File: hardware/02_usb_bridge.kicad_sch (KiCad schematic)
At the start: 73 parts, among them J201 PCB pads (no component), J202 PCB pads (no component), Q207 AO3400A, U201 CH32V307RCT6, U202 AGRV2KQ32, U205 74LVC1G157, U206 74LVC1G11, U208 74LVC3G34, X201 80.000 MHz, X202 49.152 MHz, X203 45.1584 MHz, Y201 8 MHz

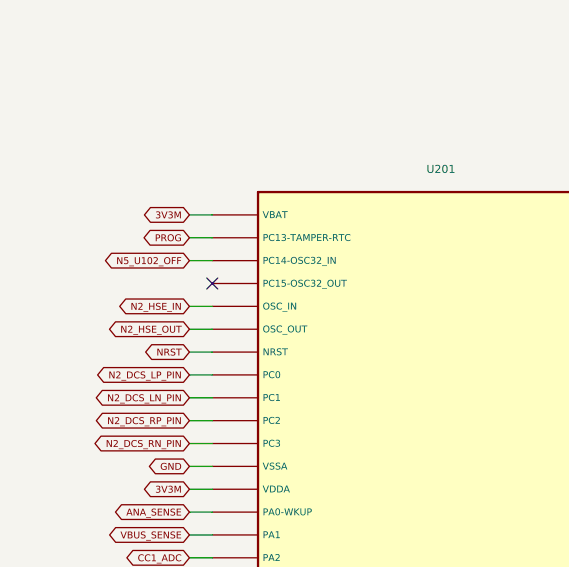
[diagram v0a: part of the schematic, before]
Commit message: Recapture DAC-HPA schematic for design set v1.1
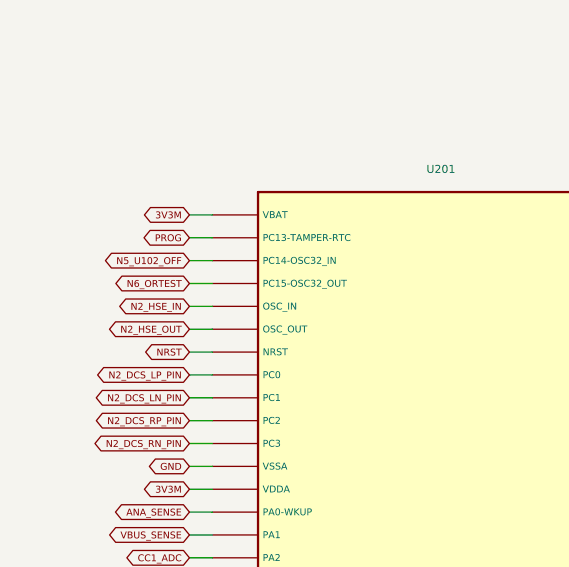
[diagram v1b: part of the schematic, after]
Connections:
- net N6_ORTEST: now reaches U201.4 (PC15-OSC32_OUT)
- no-connect marks 12 -> 11
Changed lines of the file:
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@@
 (generator_version "10.0")
 (paper "A2")
-(title_block (title "2  USB AUDIO BRIDGE / CPLD / CLOCKS") (date "2026-09-26") (rev "Schematic capture v1.0") (comment 1 "REVIEW ONLY: G-1 to G-4 and J702 contact map remain open"))
+(title_block (title "2  USB AUDIO BRIDGE / CPLD / CLOCKS") (date "2026-09-27") (rev "v1.1") (comment 1 "Design Spec v1.1 / Notes v1.0 / Parts List v0.9") (comment 2 "REVIEW ONLY: G-1 to G-4 remain open; J701/J702 maps from maker drawings"))
 (text "2  USB AUDIO BRIDGE / CPLD / CLOCKS" (exclude_from_sim no) (at 20.32 15.24 0) (effects (font (size 1.524 1.524)) (justify left bottom)))
 (symbol (lib_id "DAC_HPA:P020") (at 50.8 217.17 0) (unit 1) (exclude_from_sim no) (in_bom yes) (on_board yes) (dnp no)
@@
 (wire (pts (xy 41.91 68.58) (xy 39.37 68.58)) (stroke (width 0) (type solid)))
 (global_label "N5_U102_OFF" (shape bidirectional) (at 39.37 68.58 180) (effects (font (size 0.762 0.762)) (justify right bottom)))
-(no_connect (at 41.91 71.12))
+(wire (pts (xy 41.91 71.12) (xy 39.37 71.12)) (stroke (width 0) (type solid)))
+(global_label "N6_ORTEST" (shape bidirectional) (at 39.37 71.12 180) (effects (font (size 0.762 0.762)) (justify right bottom)))
 (wire (pts (xy 41.91 73.66) (xy 39.37 73.66)) (stroke (width 0) (type solid)))
 (global_label "N2_HSE_IN" (shape bidirectional) (at 39.37 73.66 180) (effects (font (size 0.762 0.762)) (justify right bottom)))
